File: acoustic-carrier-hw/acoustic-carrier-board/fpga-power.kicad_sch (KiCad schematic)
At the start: 15 parts, among them IC1 ECP5-BGA256

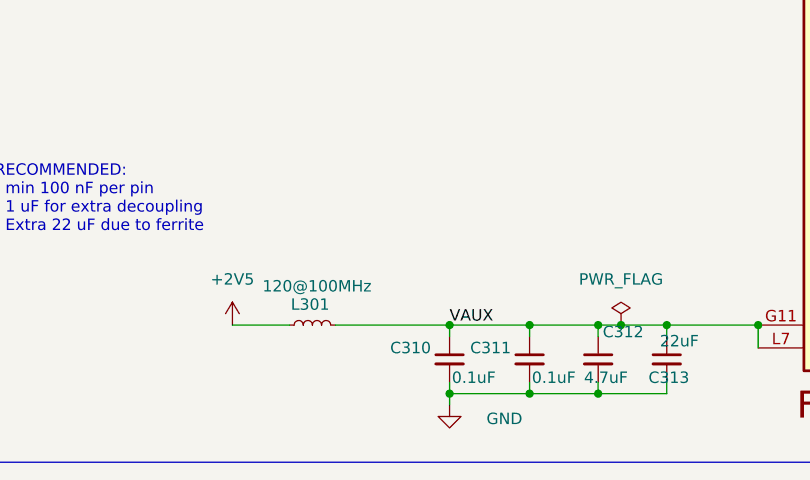
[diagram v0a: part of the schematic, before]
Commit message: [carrier] Added extra decoupling to ADC bias voltage
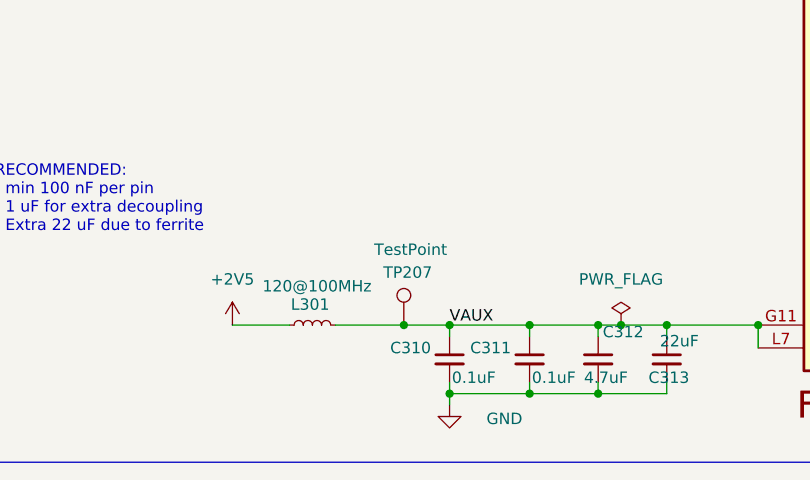
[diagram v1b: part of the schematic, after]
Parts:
- added TP207: TestPoint, TestPoint:TestPoint_Loop_D1.80mm_Drill1.0mm_Beaded, symbol Connector:TestPoint
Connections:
- net VAUX: now also TP207.1
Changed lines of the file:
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@@
 	)
 	(junction
+		(at 137.16 124.46)
+		(diameter 0)
+		(color 0 0 0 0)
+	)
+	(junction
 		(at 214.63 114.3)
 		(diameter 0)
@@
 	(wire
 		(pts
+			(xy 137.16 124.46) (xy 142.24 124.46)
+		)
+		(stroke
+			(width 0)
+			(type default)
+		)
+	)
+	(wire
+		(pts
 			(xy 130.81 68.58) (xy 138.43 68.58)
 		)
@@
 	(wire
 		(pts
-			(xy 129.54 124.46) (xy 142.24 124.46)
+			(xy 129.54 124.46) (xy 137.16 124.46)
 		)
 		(stroke
@@
 					(unit 1)
 				)
+			)
+		)
+	)
+	(symbol
+		(lib_id "Connector:TestPoint")
+		(at 137.16 124.46 0)
+		(unit 1)
+		(exclude_from_sim no)
+		(in_bom yes)
+		(on_board yes)
+		(dnp no)
+		(property "Reference" "TP207"
+			(at 134.874 118.618 0)
+			(effects
+				(font
+					(size 1.27 1.27)
+				)
+				(justify left)
+			)
+		)
+		(property "Value" "TestPoint"
+			(at 133.858 116.078 0)
+			(effects
+				(font
+					(size 1.27 1.27)
+				)
+				(justify left)
+			)
+		)
+		(property "Footprint" "TestPoint:TestPoint_Loop_D1.80mm_Drill1.0mm_Beaded"
+			(at 142.24 124.46 0)
+			(effects
+				(font
+					(size 1.27 1.27)
+				)
+				(hide yes)
+			)
+		)
+		(property "Datasheet" "~"
+			(at 142.24 124.46 0)
+			(effects
+				(font
+					(size 1.27 1.27)
+				)
+				(hide yes)
+			)
+		)
+		(property "Description" "test point"
+			(at 137.16 124.46 0)
+			(effects
+				(font
+					(size 1.27 1.27)
+				)
+				(hide yes)
+			)
+		)
+		(pin "1"
+		)
+		(instances
+			(project "acoustic-carrier-board"
+				(path "/25b015c9-ab13-4427-b72c-b6f348597100/aad6bec2-3cac-4ef0-abf0-8e1f80301155"
+					(reference "TP207")
+					(unit 1)
+				)

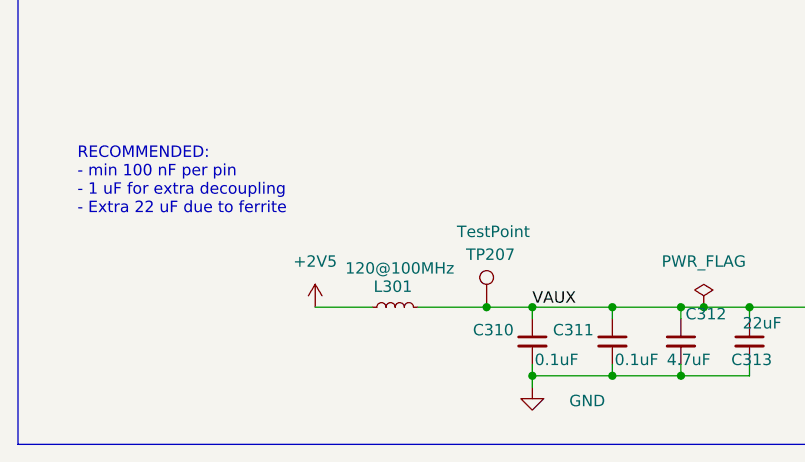
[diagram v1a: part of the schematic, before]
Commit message: [carrier] finished for production (next) reroute the LPDDR3, with appropriate CMD-CTRL bus delays, and change banks for command-control
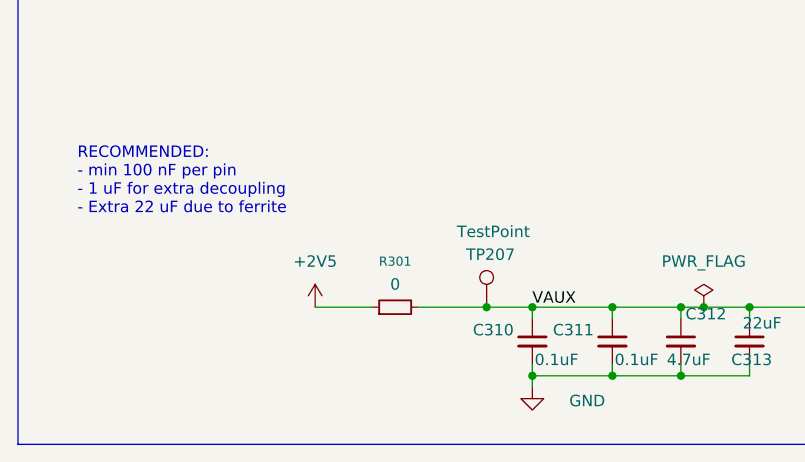
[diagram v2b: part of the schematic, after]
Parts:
- removed L301: 120@100MHz, Inductor_SMD:L_0603_1608Metric, symbol Device:L_Small
- added R301: 0, Resistor_SMD:R_0805_2012Metric_Pad1.20x1.40mm_HandSolder, symbol Device:R_Small
- IC1: Manufacturer Lattice -> (none)
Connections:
- net +2V5: now also R301.1
- net VAUX: now also R301.2
